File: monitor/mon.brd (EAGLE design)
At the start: 50 x 24 mm, 16 parts

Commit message: monitor done
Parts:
- moved C4 66.7 mm to (45.2, 14.2), flipped to the bottom, turned to 270 degrees
- moved C3 65.6 mm to (46.7, 14.2), flipped to the bottom, turned to 270 degrees
- moved R1 61.2 mm to (43.7, 14.2), flipped to the bottom, turned to 270 degrees
- moved C7 54.5 mm to (17.8, 7.62), turned to 180 degrees
- moved C5 53.0 mm to (17.5, 12.2), turned to 180 degrees
- moved C6 50.2 mm to (17.8, 6.10), turned to 180 degrees
- moved C2 49.4 mm to (29.5, 14.0), flipped to the bottom
- moved C1 45.3 mm to (26.7, 14.0), flipped to the bottom
- moved ESP8266 37.5 mm to (28.4, 19.6), flipped to the bottom, turned to 0 degrees
- moved IC1 27.8 mm to (11.7, 7.87), flipped to the top, turned to 270 degrees
- moved U$1 11.4 mm to (17.5, 16.3), flipped to the top, turned to 90 degrees
- moved U$4 3.18 mm to (42.9, 19.6), turned to 0 degrees
- moved JP1 3.05 mm to (1.52, 9.65), flipped to the top, turned to 270 degrees
- moved U$2 0.76 mm to (6.35, 1.52)
- moved J$1 0.57 mm to (2.29, 21.1)
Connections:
- net GND: now also J$1.GND@0, J$1.GND@1, J$1.GND@2, J$1.GND@3
- net UART_RX: now also ESP8266.1; no longer ESP8266.8
- net UART_TX: now also ESP8266.8; no longer ESP8266.1
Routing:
- net VCC: track 0.00 -> 73.6 mm, vias 0 -> 1
- net MOSI: track 0.00 -> 44.8 mm, vias 0 -> 2
- net SCK: track 0.00 -> 43.7 mm, vias 0 -> 1
- net SWDAT: track 0.00 -> 42.6 mm, vias 0 -> 1
- net SWCLK: track 0.00 -> 38.0 mm, vias 0 -> 1
- net UART_RX: track 0.00 -> 34.8 mm, vias 0 -> 1
- net DISPLAY_DC: track 0.00 -> 29.6 mm, vias 0 -> 1
- net DISPLAY_CS: track 0.00 -> 27.6 mm, vias 0 -> 1
- net DISPLAY_RST: track 0.00 -> 27.3 mm, vias 0 -> 1
- net NRST: track 0.00 -> 24.2 mm, vias 0 -> 1
- net UART_TX: track 0.00 -> 23.6 mm, vias 0 -> 1
- net N$2: track 0.00 -> 19.7 mm
- net N$1: track 0.00 -> 8.84 mm
- net MISO: track 0.00 -> 7.92 mm, vias 0 -> 1
- net GND: track 0.00 -> 7.73 mm, vias 0 -> 55
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- added copper zone on layer 1, net GND
- added copper zone on layer 16, net GND
- added copper zone on layer 1, net VCC
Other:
- outline, holes or cut-outs redrawn
- board text added: "3V3"
- board text added: "4.5-20V"
- board text added: "ESP8266"
- board text added: "JON SOWMAN"
- board text added: "MAR 2015"
- board text added: "OLED"
- board text added: "RFM69"
- board text added: "UKHASnet"

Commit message: tidying mon
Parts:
- moved JP1 0.76 mm to (1.52, 8.89)
- moved U$3 0.57 mm to (23.1, 3.56)
- moved C3 0.51 mm to (46.2, 14.2)
- moved C4 0.25 mm to (45.0, 14.2)
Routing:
- net N$2: track 19.7 -> 21.6 mm
- net SCK: track 43.7 -> 43.0 mm
- net MOSI: track 44.8 -> 44.0 mm
- net DISPLAY_DC: track 29.6 -> 28.9 mm
- net DISPLAY_RST: track 27.3 -> 26.5 mm
- net DISPLAY_CS: track 27.6 -> 26.8 mm
- net N$7: track 3.74 -> 3.02 mm
- net N$4: track 4.17 -> 3.56 mm
- net N$3: track 4.46 -> 3.85 mm
- net N$9: track 3.71 -> 3.15 mm
- net GND: track 7.73 -> 7.22 mm, vias 55 -> 57
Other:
- outline, holes or cut-outs redrawn

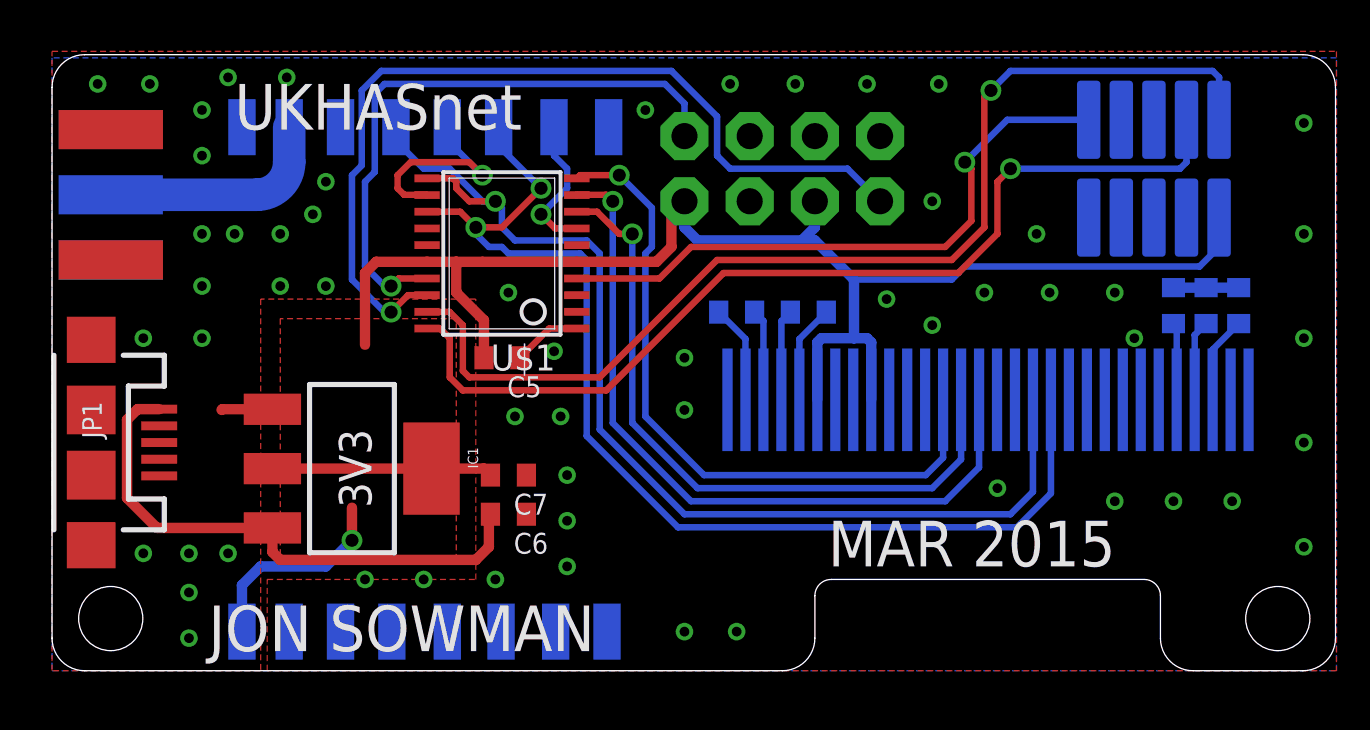
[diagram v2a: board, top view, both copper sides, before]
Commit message: routed wh1080 txer
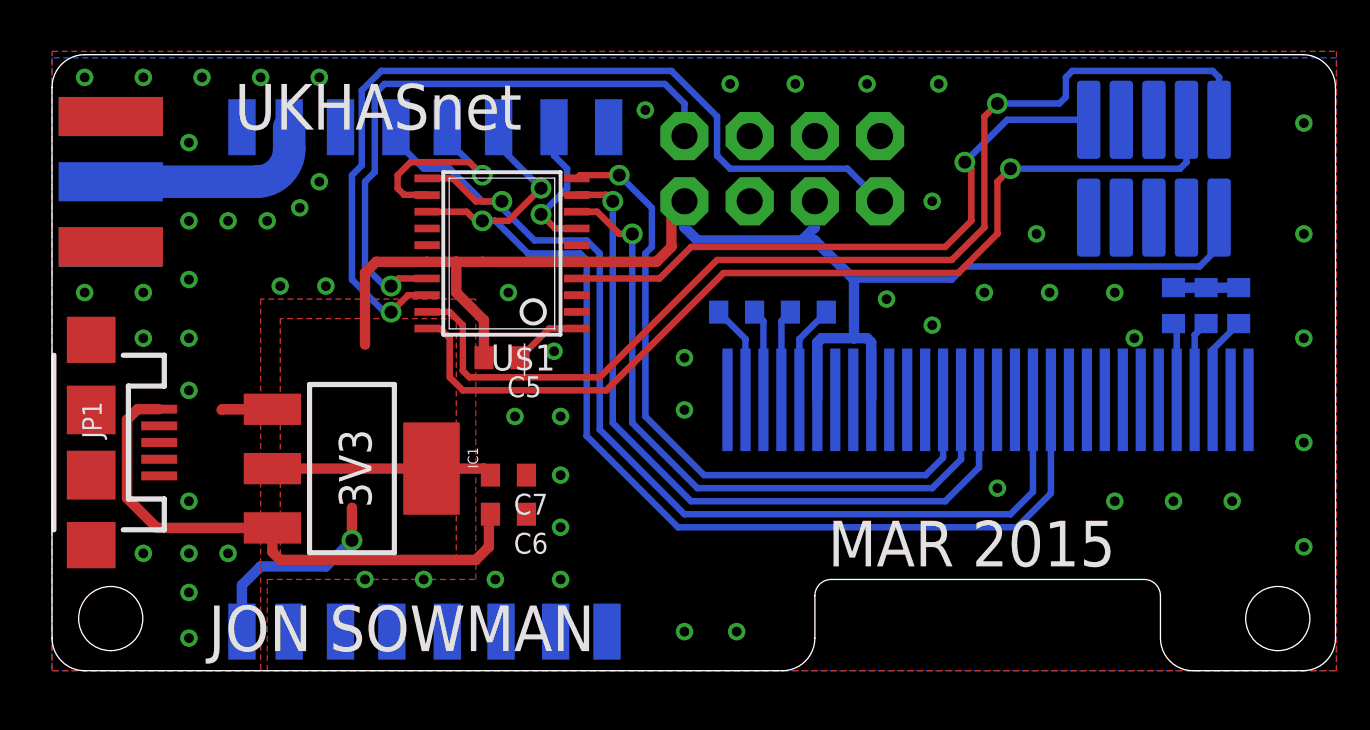
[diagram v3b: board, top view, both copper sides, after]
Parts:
- moved J$1 0.51 mm to (2.29, 21.6)
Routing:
- net N$1: track 8.84 -> 8.33 mm
- net MOSI: track 44.0 -> 43.5 mm
- net GND: vias 57 -> 61
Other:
- board text added: "SWD"
